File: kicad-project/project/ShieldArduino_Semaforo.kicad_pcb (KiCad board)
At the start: 2 copper layers, 68.6 x 53.3 mm, 21 parts, among them P1 Power, P2 Analog, P3 Digital, P4 Digital, P5 CONN_01X01, P6 CONN_01X01, P7 CONN_01X01, P8 CONN_01X01, SW1 SW_Push

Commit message: shield-prototype-v1.2
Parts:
- removed D1, D2, D3: LED, LED_THT:LED_D3.0mm
- removed D4, D5: LED, LED_THT:LED_D1.8mm_W3.3mm_H2.4mm
- removed SW1: SW_Push, Button_Switch_THT:SW_PUSH_6mm
- added C1: 100n, Capacitor_SMD:C_0805_2012Metric_Pad1.18x1.45mm_HandSolder, F.Cu at (128.5, 105.2)
- added C116: 100nF, Capacitor_SMD:C_0603_1608Metric_Pad1.08x0.95mm_HandSolder, F.Cu at (139.8, 88.8)
- added C117: 100nF, Capacitor_SMD:C_0603_1608Metric_Pad1.08x0.95mm_HandSolder, F.Cu at (139.8, 91.3)
- added C2: 6.8u, Capacitor_SMD:C_0805_2012Metric_Pad1.18x1.45mm_HandSolder, F.Cu at (128.5, 108.2)
- added C3: 47u, Capacitor_SMD:C_1210_3225Metric_Pad1.33x2.70mm_HandSolder, F.Cu at (133.9, 105.8)
- added D7: ESDA5V3SC5, Package_TO_SOT_SMD:SOT-23-5, F.Cu at (158.6, 89.9)
- added IC1: TPS54302DDCR, footprint:SOT95P280X110-6N, F.Cu at (133.2, 110.3)
- added J1: Conn_01x10, footprint:M80-50010YY_2, B.Cu at (118.5, 96.9)
- added L1: 10u, Inductor_SMD:L_Bourns-SRN8040_8x8.15mm, F.Cu at (131.0, 98.8)
- added R6: 10k, Resistor_SMD:R_0603_1608Metric_Pad0.98x0.95mm_HandSolder, F.Cu at (144.1, 91.3)
- added R7: 5.2K, Resistor_SMD:R_0603_1608Metric_Pad0.98x0.95mm_HandSolder, F.Cu at (144.1, 93.8)
- added R8: 10k, Resistor_SMD:R_0603_1608Metric_Pad0.98x0.95mm_HandSolder, F.Cu at (144.1, 96.3)
- added R9: 10k, Resistor_SMD:R_0603_1608Metric_Pad0.98x0.95mm_HandSolder, F.Cu at (144.1, 98.8)
- added U2: LM321, Package_TO_SOT_SMD:SOT-23-5, F.Cu at (158.6, 94.5)
- added U4: MCP2542FD-E/MF, Package_DFN_QFN:DFN-8-1EP_3x3mm_P0.65mm_EP1.55x2.4mm, F.Cu at (160.2, 99.6)
- R1: value R -> 100k; footprint Resistor_SMD:R_2010_5025Metric -> Resistor_SMD:R_0603_1608Metric_Pad0.98x0.95mm_HandSolder
- R2: value R -> 13.7k; footprint Resistor_SMD:R_2010_5025Metric -> Resistor_SMD:R_0603_1608Metric_Pad0.98x0.95mm_HandSolder
- R3, R5: value R -> 5k; footprint Resistor_SMD:R_2010_5025Metric -> Resistor_SMD:R_0603_1608Metric_Pad0.98x0.95mm_HandSolder
- R4: value R -> 10k; footprint Resistor_SMD:R_2010_5025Metric -> Resistor_SMD:R_0603_1608Metric_Pad0.98x0.95mm_HandSolder
- moved R1 20.1 mm to (122.6, 107.3)
- moved R5 19.3 mm to (144.1, 88.8)
- moved R2 15.9 mm to (122.6, 109.8)
- moved R3 13.2 mm to (139.8, 98.8)
- moved R4 5.24 mm to (139.8, 101.3)
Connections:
- P1 pad 1: (no net) -> unconnected-(P1-Pin_1-Pad1)
- P1 pad 2: (no net) -> /IOREF
- P1 pad 3: (no net) -> /Reset
- P1 pad 4: (no net) -> +3V3
- P1 pad 8: (no net) -> /Vin
- P2 pad 1: (no net) -> /pedal_out
- P2 pad 2: (no net) -> /brake_out
- P2 pad 3: (no net) -> /Analog_pedal_stm_out
- P2 pad 4: (no net) -> /A3
- P3 pad 1: /A5(SCL) -> /CAN_RX
- P3 pad 2: /A4(SDA) -> /CAN_TX
- P3 pad 3: (no net) -> /AREF
- P3 pad 5: (no net) -> /13(SCK)
- P3 pad 6: (no net) -> /12(MISO)
- P3 pad 7: (no net) -> /11(**/MOSI)
- P3 pad 8: (no net) -> /10(**/SS)
- P4 pad 4: (no net) -> /4
- P4 pad 5: (no net) -> /3(**)
- P4 pad 7: (no net) -> /1(Tx)
- P4 pad 8: (no net) -> /0(Rx)
- P5 pad 1: (no net) -> unconnected-(P5-Pin_1-Pad1)
- P6 pad 1: (no net) -> unconnected-(P6-Pin_1-Pad1)
- P7 pad 1: (no net) -> unconnected-(P7-Pin_1-Pad1)
- P8 pad 1: (no net) -> unconnected-(P8-Pin_1-Pad1)
- R1 pad 2: /7 -> Net-(IC1-FB)
- R2 pad 1: Net-(D2-Pad2) -> Net-(IC1-FB)
- R2 pad 2: /9(**) -> GND
- R3 pad 1: Net-(D3-Pad2) -> /pedal_in
- R3 pad 2: /8 -> /pedal_out
- R4 pad 1: Net-(D4-Pad2) -> /pedal_out
- R4 pad 2: /5(**) -> GND
- R5 pad 1: Net-(D5-Pad2) -> /brake_in
- R5 pad 2: /6(**) -> /brake_out
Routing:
- net /A5(SCL): track 70.1 -> 1.81 mm, vias 2 -> 0
- net /A4(SDA): track 64.7 -> 0.15 mm
- net /8: track 42.7 -> 0.24 mm, vias 2 -> 0
- net /6(**): track 41.8 -> 0.45 mm, vias 2 -> 0
- net +5V: track 35.7 -> 0.00 mm
- net /5(**): track 34.2 -> 0.00 mm
- net /9(**): track 33.7 -> 0.01 mm, vias 2 -> 0
- net /7: track 27.3 -> 0.00 mm
- net /2: track 26.0 -> 0.68 mm
- net Net-(C3-Pad1): track 19.0 -> 0.00 mm
- net Net-(D3-Pad2): track 18.9 -> 0.00 mm
- net Net-(D2-Pad2): track 17.3 -> 0.00 mm
- net Net-(D4-Pad2): track 9.77 -> 0.00 mm
- net Net-(D5-Pad2): track 9.32 -> 0.00 mm

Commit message: pcb-tweaks
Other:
- board text removed: "Diseñado por Piensa 3D 2018"
- board text removed: "Shield de semáforo para Arduino UNO"
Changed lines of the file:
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@@
 		(layer "Edge.Cuts")
-	)
-	(gr_text "Diseñado por\nPiensa 3D\n2018"
-		(at 119.773 81.965 0)
-		(layer "F.SilkS")
-		(effects
-			(font
-				(size 1.5 1.5)
-				(thickness 0.3)
-			)
-		)
 	)
 	(gr_text "1"
@@
 			)
 		)
-	)
-	(gr_text "Shield de semáforo para \nArduino UNO"
-		(at 149.073 118.54 0)
-		(layer "F.SilkS")
-		(effects
-			(font
-				(size 1.5 1.5)
-				(thickness 0.3)
-			)
-		)

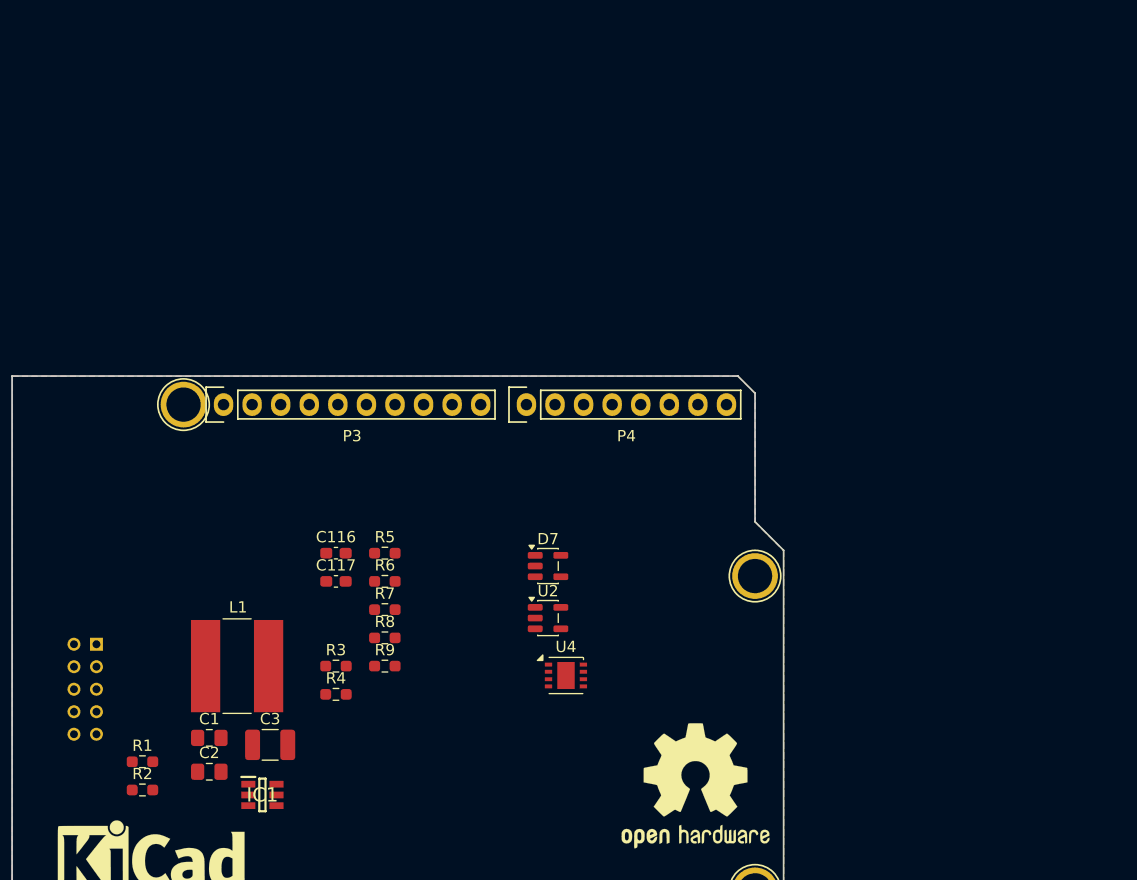
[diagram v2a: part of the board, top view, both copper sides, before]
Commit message: kicad-reverse_polarity_pinout_tvs-update
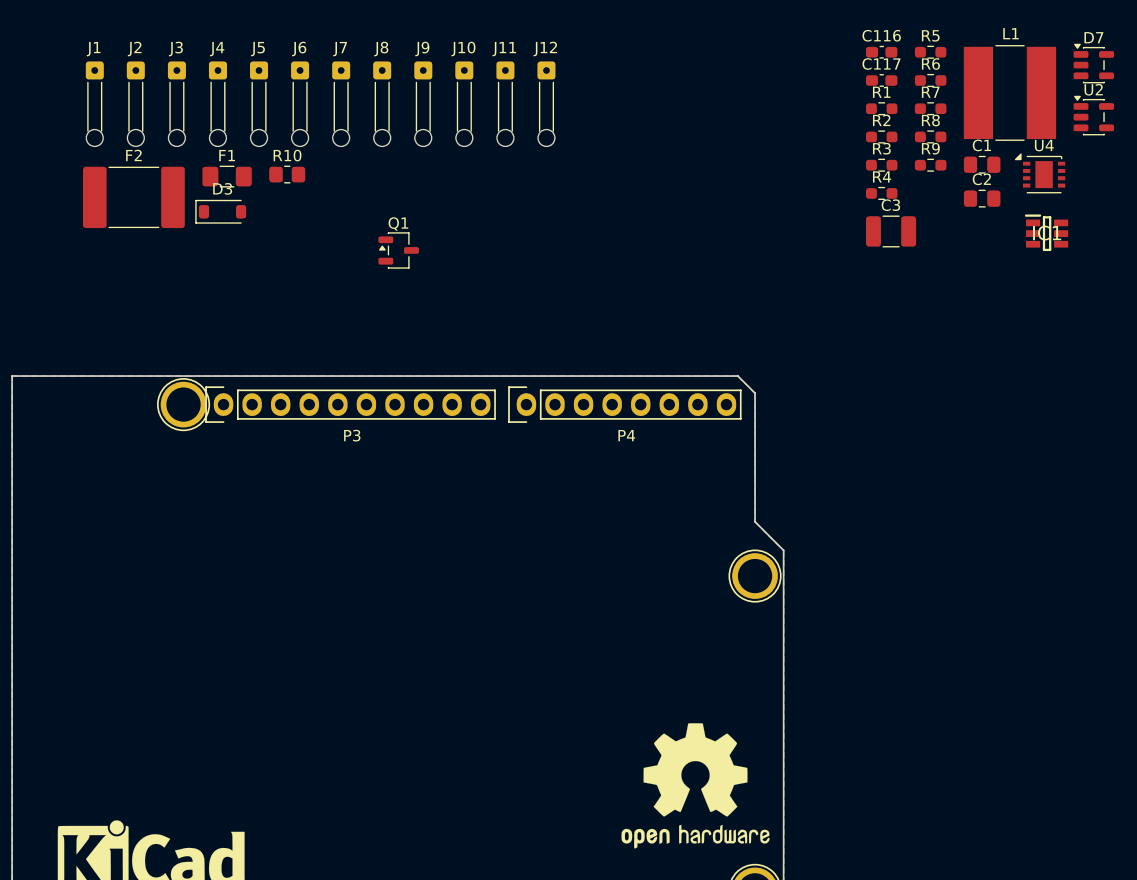
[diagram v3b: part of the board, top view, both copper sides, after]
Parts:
- added D3: Schottky, Diode_SMD:D_SOD-123, F.Cu at (129.7, 58.4)
- added F1: 0.5A, Fuse:Fuse_1206_3216Metric_Pad1.42x1.75mm_HandSolder, F.Cu at (130.1, 55.3)
- added F2: 1A, Fuse:Fuse_2920_7451Metric_Pad2.10x5.45mm_HandSolder, F.Cu at (121.8, 57.1)
- added J10: Conn_01x01, Connector_Wire:SolderWire-0.1sqmm_1x01_D0.4mm_OD1mm_Relief, F.Cu at (151.2, 45.9)
- added J11: Conn_01x01, Connector_Wire:SolderWire-0.1sqmm_1x01_D0.4mm_OD1mm_Relief, F.Cu at (154.8, 45.9)
- added J12: Conn_01x01, Connector_Wire:SolderWire-0.1sqmm_1x01_D0.4mm_OD1mm_Relief, F.Cu at (158.5, 45.9)
- added J2: Conn_01x01, Connector_Wire:SolderWire-0.1sqmm_1x01_D0.4mm_OD1mm_Relief, F.Cu at (122.0, 45.9)
- added J3: Conn_01x01, Connector_Wire:SolderWire-0.1sqmm_1x01_D0.4mm_OD1mm_Relief, F.Cu at (125.6, 45.9)
- added J4: Conn_01x01, Connector_Wire:SolderWire-0.1sqmm_1x01_D0.4mm_OD1mm_Relief, F.Cu at (129.3, 45.9)
- added J5: Conn_01x01, Connector_Wire:SolderWire-0.1sqmm_1x01_D0.4mm_OD1mm_Relief, F.Cu at (132.9, 45.9)
- added J6: Conn_01x01, Connector_Wire:SolderWire-0.1sqmm_1x01_D0.4mm_OD1mm_Relief, F.Cu at (136.6, 45.9)
- added J7: Conn_01x01, Connector_Wire:SolderWire-0.1sqmm_1x01_D0.4mm_OD1mm_Relief, F.Cu at (140.2, 45.9)
- added J8: Conn_01x01, Connector_Wire:SolderWire-0.1sqmm_1x01_D0.4mm_OD1mm_Relief, F.Cu at (143.9, 45.9)
- added J9: Conn_01x01, Connector_Wire:SolderWire-0.1sqmm_1x01_D0.4mm_OD1mm_Relief, F.Cu at (147.5, 45.9)
- added Q1: PMOS, Package_TO_SOT_SMD:SOT-23-3, F.Cu at (145.4, 61.9)
- added R10: 100k, Resistor_SMD:R_0805_2012Metric_Pad1.20x1.40mm_HandSolder, F.Cu at (135.5, 55.1)
- J1: value Conn_01x10 -> Conn_01x01; footprint footprint:M80-50010YY_2 -> Connector_Wire:SolderWire-0.1sqmm_1x01_D0.4mm_OD1mm_Relief; moved to F.Cu
- moved R1 87.7 mm to (188.3, 49.3)
- moved R2 87.7 mm to (188.3, 51.8)
- moved IC1 85.8 mm to (203.0, 60.4)
- moved C1 85.5 mm to (197.2, 54.2)
- moved C2 85.5 mm to (197.2, 57.3)
- moved L1 85.5 mm to (199.7, 47.9)
- moved C3 71.6 mm to (189.1, 60.2)
- moved C116 65.8 mm to (188.3, 44.2)
- moved C117 65.8 mm to (188.3, 46.8)
- moved D7 65.8 mm to (207.1, 45.4)
- moved R3 65.8 mm to (188.3, 54.3)
- moved R4 65.8 mm to (188.3, 56.8)
- moved R5 65.8 mm to (192.6, 44.2)
- moved R6 65.8 mm to (192.6, 46.8)
- moved R7 65.8 mm to (192.6, 49.3)
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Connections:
- net /Analog_pedal_stm_out renamed /inverter_signal_3V3
- net /brake_out renamed /brake_in_3V3
- net /pedal_in renamed /throttle_in
- net /pedal_out renamed /throttle_in_3V3
- P4 pad 7: /1(Tx) -> /UART_RX
- P4 pad 8: /0(Rx) -> /UART_TX
- R7 pad 2: /analog_engine -> /inverter_signal_5V
- U2 pad 4: /analog_engine -> /inverter_signal_5V

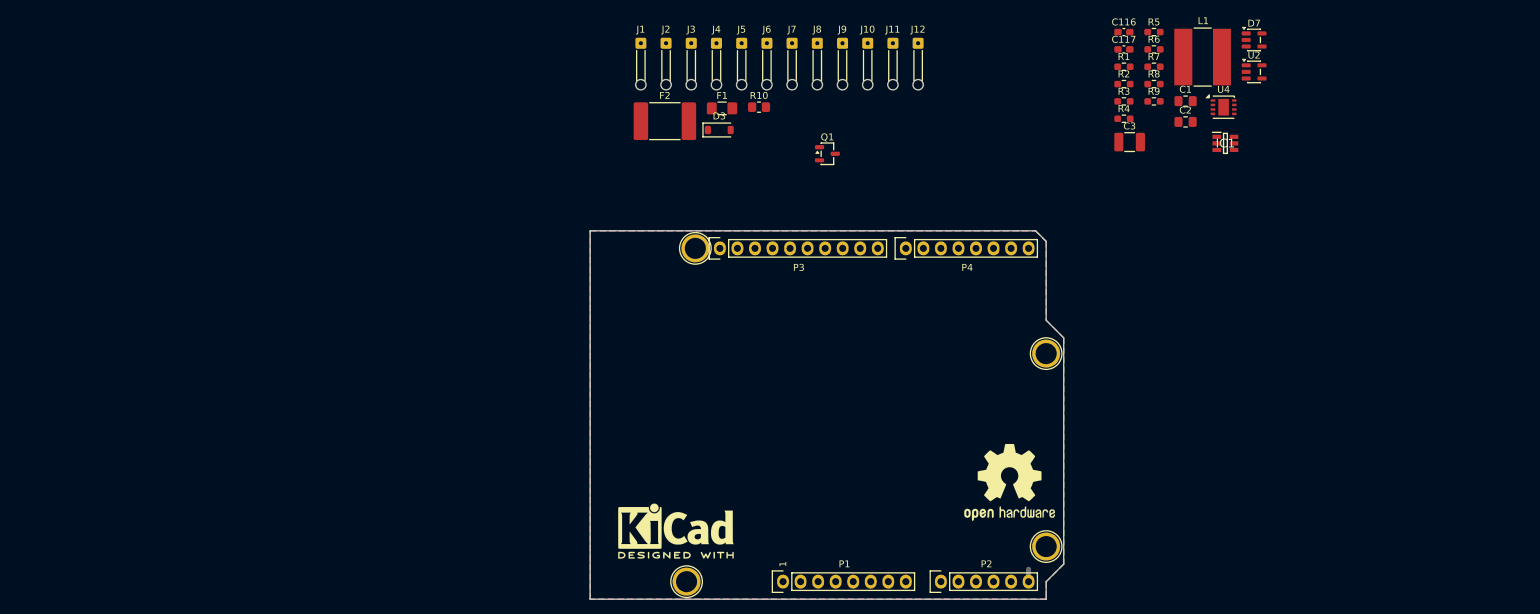
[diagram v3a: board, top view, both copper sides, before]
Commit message: kicad-tvs_psu_pinout-update
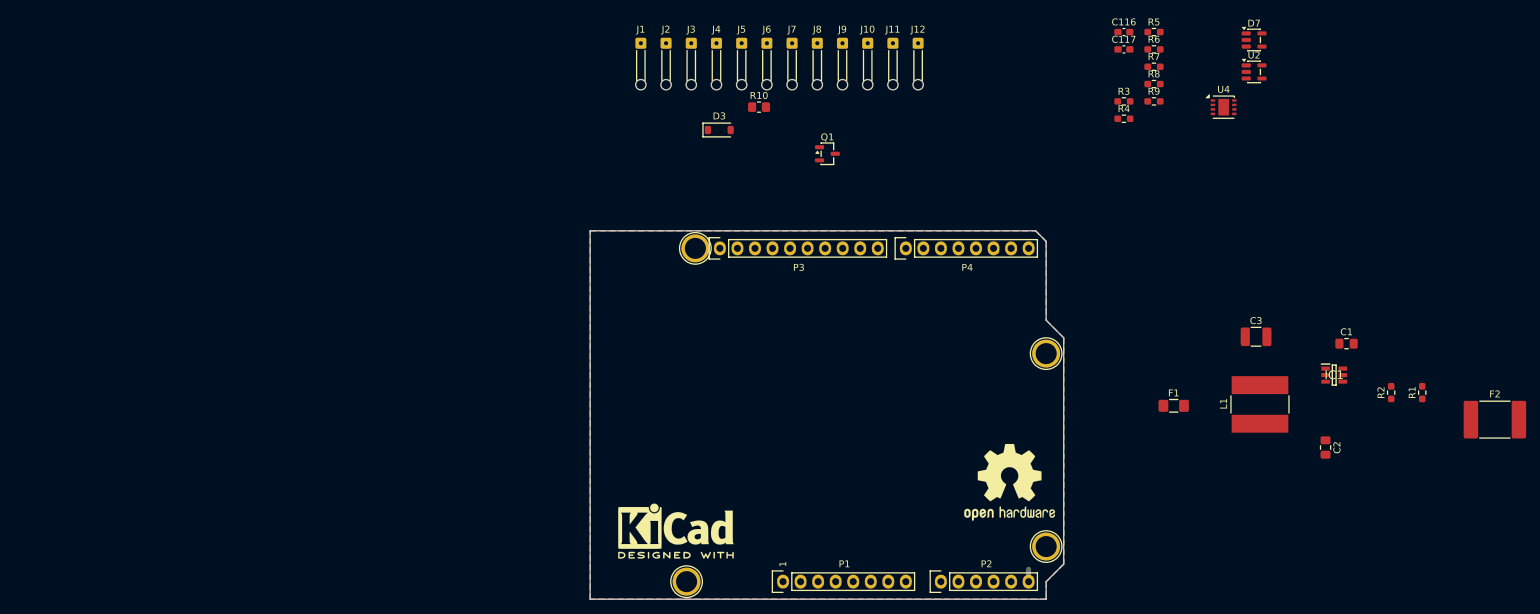
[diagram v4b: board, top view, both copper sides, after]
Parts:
- moved F2 127.7 mm to (242.0, 100.4)
- moved F1 78.3 mm to (195.5, 98.4)
- moved R1 64.0 mm to (231.5, 96.5), turned to 90 degrees
- moved R2 59.1 mm to (227.0, 96.5), turned to 90 degrees
- moved C2 51.3 mm to (217.5, 104.4), turned to -90 degrees
- moved L1 51.0 mm to (208.0, 98.2), turned to 90 degrees
- moved C1 42.2 mm to (220.5, 89.4)
- moved IC1 37.1 mm to (218.7, 93.9)
- moved C3 33.6 mm to (207.4, 88.4)

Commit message: pcb-tests
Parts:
- removed the C1 at (220.5, 89.4)
- removed the R1 at (231.5, 96.5)
- removed the R2 at (227.0, 96.5)
- added C10: 22u, Capacitor_SMD:C_0603_1608Metric_Pad1.08x0.95mm_HandSolder, F.Cu at (131.6, 89.2)
- added C11: 22u, Capacitor_SMD:C_0603_1608Metric_Pad1.08x0.95mm_HandSolder, F.Cu at (131.6, 91.7)
- added C119: 10u, Capacitor_SMD:C_0805_2012Metric_Pad1.18x1.45mm_HandSolder, F.Cu at (121.1, 97.4)
- added C12: 1uF, Capacitor_SMD:C_0603_1608Metric_Pad1.08x0.95mm_HandSolder, F.Cu at (131.6, 94.2)
- added C120: 10uf, Capacitor_SMD:C_0805_2012Metric_Pad1.18x1.45mm_HandSolder, F.Cu at (121.0, 100.2)
- added C121: 100n 280mOhm, Capacitor_SMD:C_0805_2012Metric_Pad1.18x1.45mm_HandSolder, F.Cu at (118.8, 88.1)
- added C122: 22u, Capacitor_SMD:C_0603_1608Metric_Pad1.08x0.95mm_HandSolder, F.Cu at (118.3, 101.6)
- added C123: 22u, Capacitor_SMD:C_0603_1608Metric_Pad1.08x0.95mm_HandSolder, F.Cu at (116.1, 101.6)
- added C5: 1uF, Capacitor_SMD:C_0603_1608Metric_Pad1.08x0.95mm_HandSolder, F.Cu at (131.6, 86.7)
- added C6: 10u, Capacitor_SMD:C_0805_2012Metric_Pad1.18x1.45mm_HandSolder, F.Cu at (136.1, 84.5)
- added C7: 3.9uF, Capacitor_SMD:C_1206_3216Metric_Pad1.33x1.80mm_HandSolder, F.Cu at (71.9, 71.0)
- added C8: 10uf, Capacitor_SMD:C_0805_2012Metric_Pad1.18x1.45mm_HandSolder, F.Cu at (136.1, 87.5)
- added C9: 100n 280mOhm, Capacitor_SMD:C_0805_2012Metric_Pad1.18x1.45mm_HandSolder, F.Cu at (136.1, 90.5)
- added D1: 6V, Diode_SMD:D_SMB_Handsoldering, F.Cu at (63.7, 79.8)
- added D2: 6V, Diode_SMD:D_SMB_Handsoldering, F.Cu at (63.7, 74.3)
- added D3: Diode TVS 12V, Diode_SMD:D_SOD-323F, F.Cu at (135.9, 102.9)
- added D4: 6V, Diode_SMD:D_SMB_Handsoldering, F.Cu at (63.7, 68.7)
- added D6: 24V, Package_TO_SOT_SMD:SOT-23-3, F.Cu at (51.1, 58.6)
- added D7: 24V, Package_TO_SOT_SMD:SOT-23-3, F.Cu at (51.1, 63.0)
- added D8: Schottky, Diode_SMD:D_SOD-123, F.Cu at (71.8, 79.4)
- added F3: 3A, Fuse:Fuse_0603_1608Metric_Pad1.05x0.95mm_HandSolder, F.Cu at (124.2, 92.7)
- added F3: 1A, Fuse:Fuse_0603_1608Metric_Pad1.05x0.95mm_HandSolder, F.Cu at (131.6, 99.3)
- added IC2: TPS563200DDCR, footrpint:TPS563200DDCR, F.Cu at (121.2, 92.5)
- added J11: Conn_01x01, Connector_Wire:SolderWire-0.1sqmm_1x01_D0.4mm_OD1mm_Relief, F.Cu at (63.9, 58.2)
- added J12: Conn_01x01, Connector_Wire:SolderWire-0.1sqmm_1x01_D0.4mm_OD1mm_Relief, F.Cu at (67.6, 58.2)
- added J13: Conn_01x01, Connector_Wire:SolderWire-0.1sqmm_1x01_D0.4mm_OD1mm_Relief, F.Cu at (71.2, 58.2)
- added J14: Conn_01x01, Connector_Wire:SolderWire-0.1sqmm_1x01_D0.4mm_OD1mm_Relief, F.Cu at (74.9, 58.2)
- added J15: Conn_01x01, Connector_Wire:SolderWire-0.1sqmm_1x01_D0.4mm_OD1mm_Relief, F.Cu at (60.3, 58.2)
- added K1: RELAY, footprint:PR412V4501A, F.Cu at (51.8, 53.5)
- added Q2: NMOS, Package_TO_SOT_SMD:SOT-23-3, F.Cu at (51.1, 67.5)
- added Q3: NMOS, Package_TO_SOT_SMD:SOT-23-3, F.Cu at (51.1, 76.4)
- added Q4: NMOS, Package_TO_SOT_SMD:SOT-23-3, F.Cu at (51.1, 71.9)
- added Q5: NMOS, Package_TO_SOT_SMD:SOT-23-3, F.Cu at (51.1, 80.8)
- added R10: 10k, Resistor_SMD:R_0805_2012Metric_Pad1.20x1.40mm_HandSolder, F.Cu at (56.1, 72.6)
- added R12: 56.2k 50mW, Resistor_SMD:R_0603_1608Metric_Pad0.98x0.95mm_HandSolder, F.Cu at (131.6, 101.8)
- added R13: 10k 50mW, Resistor_SMD:R_0603_1608Metric_Pad0.98x0.95mm_HandSolder, F.Cu at (131.6, 104.3)
- added R15: 100, Resistor_SMD:R_0805_2012Metric_Pad1.20x1.40mm_HandSolder, F.Cu at (56.1, 63.7)
- added R165: 56.2k 50mW, Resistor_SMD:R_0603_1608Metric_Pad0.98x0.95mm_HandSolder, F.Cu at (119.1, 83.9)
- added R166: 10k 50mW, Resistor_SMD:R_0603_1608Metric_Pad0.98x0.95mm_HandSolder, F.Cu at (119.1, 85.8)
- added R17: 10k, Resistor_SMD:R_0805_2012Metric_Pad1.20x1.40mm_HandSolder, F.Cu at (56.1, 66.7)
- added R18: 100, Resistor_SMD:R_0805_2012Metric_Pad1.20x1.40mm_HandSolder, F.Cu at (56.1, 75.5)
- added R20: 10k, Resistor_SMD:R_0805_2012Metric_Pad1.20x1.40mm_HandSolder, F.Cu at (56.1, 78.5)
- added R3: 200, Resistor_SMD:R_0603_1608Metric_Pad0.98x0.95mm_HandSolder, F.Cu at (71.1, 73.9)
- added R6: 200, Resistor_SMD:R_0603_1608Metric_Pad0.98x0.95mm_HandSolder, F.Cu at (71.1, 76.4)
- added R7: 100, Resistor_SMD:R_0805_2012Metric_Pad1.20x1.40mm_HandSolder, F.Cu at (56.1, 57.8)
- added R8: 100, Resistor_SMD:R_0805_2012Metric_Pad1.20x1.40mm_HandSolder, F.Cu at (56.1, 69.6)
- added R9: 10k, Resistor_SMD:R_0805_2012Metric_Pad1.20x1.40mm_HandSolder, F.Cu at (56.1, 60.8)
- added TP1: TestPoint_Small, TestPoint:TestPoint_Pad_D1.0mm, F.Cu at (135.3, 93.5)
- added TP2: TestPoint_Small, TestPoint:TestPoint_Pad_D1.0mm, F.Cu at (135.3, 96.6)
- C2: value 6.8u -> 3.9uF; footprint Capacitor_SMD:C_0805_2012Metric_Pad1.18x1.45mm_HandSolder -> Capacitor_SMD:C_1206_3216Metric_Pad1.33x1.80mm_HandSolder
- C3: value 47u -> 1uF; footprint Capacitor_SMD:C_1210_3225Metric_Pad1.33x2.70mm_HandSolder -> Capacitor_SMD:C_0603_1608Metric_Pad1.08x0.95mm_HandSolder
- F1: value 0.5A -> 3A; footprint Fuse:Fuse_1206_3216Metric_Pad1.42x1.75mm_HandSolder -> Fuse:Fuse_0603_1608Metric_Pad1.05x0.95mm_HandSolder
- F2: value 1A -> 0.5A; footprint Fuse:Fuse_2920_7451Metric_Pad2.10x5.45mm_HandSolder -> Fuse:Fuse_1206_3216Metric_Pad1.42x1.75mm_HandSolder
- IC1: value TPS54302DDCR -> TPS563200DDCR; footprint footprint:SOT95P280X110-6N -> footprint:TPS563200DDCR
- L1: value 10u -> 3.3u 20mOhm; footprint Inductor_SMD:L_Bourns-SRN8040_8x8.15mm -> footprint:CLF7045__
- moved C2 150.1 mm to (71.9, 67.6), turned to 0 degrees
- moved F2 105.3 mm to (136.7, 99.7)
- moved L1 90.1 mm to (118.5, 108.9), turned to 180 degrees
- moved C3 76.0 mm to (131.6, 84.2)
- moved IC1 70.0 mm to (148.7, 95.6)
- moved F1 64.0 mm to (131.6, 96.8)
- renumbered C116 to C1, C117 to C4, D7 to D5, D3 to D9, J4 to J10, J5 to J3, J12 to J4, J6 to J5, J7 to J6, J8 to J7, J9 to J8, J3 to J9, R3 to R1, R10 to R11, R9 to R14, R8 to R16, R7 to R19, R4 to R2, R5 to R4, R6 to R5, U4 to U1
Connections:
- C2 pad 1: Net-(IC1-VIN) -> /throttle_in_3V3
- C3 pad 1: Net-(C3-Pad1) -> /12V_in_protected
- D9 pad 1: /12V_in_protected -> Net-(D9-K)
- F1 pad 2: Net-(IC1-VIN) -> +12V
- F2 pad 1: Net-(C3-Pad1) -> Net-(D9-K)
- F2 pad 2: +5V -> /12V_in_protected
- IC1 pad 3: Net-(IC1-VIN) -> +12V
- IC1 pad 5: unconnected-(IC1-EN-Pad5) -> +12V
- J6 pad 1: /5V_out -> +5V
- J7 pad 1: /5V_out -> +5V
- L1 pad 2: Net-(C3-Pad1) -> /5V_unfused
- P4 pad 3: /5(**) -> /signal_relay
- P4 pad 4: /4 -> /signal_reverse
- P4 pad 5: /3(**) -> /signal_low_speed
- P4 pad 6: /2 -> /signal_high_speed
- Q1 pad 3: /12V_in_protected -> Net-(D9-K)
- R1 pad 2: /throttle_in_3V3 -> Net-(R1-Pad2)
- R2 pad 1: /throttle_in_3V3 -> Net-(R1-Pad2)
- R4 pad 2: /brake_in_3V3 -> Net-(R4-Pad2)
- R5 pad 1: /brake_in_3V3 -> Net-(R4-Pad2)
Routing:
- net Net-(IC2-VFB): track 0.00 -> 10.8 mm
- net GND: track 0.00 -> 9.98 mm, vias 0 -> 4
- net 12V_IN: track 0.00 -> 6.05 mm
- net Net-(IC2-VBST): track 0.00 -> 3.25 mm
- net +12V: track 0.00 -> 2.89 mm
- net /Power/5V/5V_unfused: track 0.00 -> 2.77 mm
- net /signal_high_speed: track 0.00 -> 0.68 mm
- net /2: track 0.68 -> 0.00 mm
- net Net-(IC2-SW): vias 0 -> 9
- added copper zone on F.Cu, net +12V
- added copper zone on F.Cu, net 12V_IN
- added copper zone on B.Cu, net Net-(IC2-SW)
- added copper zone on F.Cu, net Net-(IC2-SW)
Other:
- board text added: "1A"
- board text added: "F2"
